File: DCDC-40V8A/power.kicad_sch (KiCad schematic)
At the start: 53 parts, among them Q1 CSD18533Q5A, Q2 CSD18533Q5A, Q3 CSD18533Q5A, Q4 CSD18533Q5A, U2 LGS5145EP, U3 MT3608, U4 GS2019-33TR5

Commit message: wip
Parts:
- added C25, C26: 100n, symbol Device:C
- added C27: 1u, symbol Device:C
- added C28, C29: 100n, Capacitor_SMD:C_0603_1608Metric, symbol Device:C
- added C30: 470n, Capacitor_SMD:C_0603_1608Metric, symbol Device:C
- added C31, C32: 100u, symbol Device:C_Polarized
- added R15, R16: 10, Resistor_SMD:R_0603_1608Metric, symbol Device:R
- C1, C8: value 22u -> 10u
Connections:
- net GND: now also C25.2, C26.2, C27.2, C28.2, C29.1, C31.2, C32.2
- net VBAT: now also C5.1
- net VCC: now also C25.1, C26.1, C27.1, C31.1, C32.1, R15.1; no longer C1.1, C2.1, C3.1, U1.30 (ACP)
- net at Q1.5 (D), R5.2: now also C1.1, C2.1, C3.1, R16.1; no longer U1.29 (ACN)
- net at C6.1, C7.1, C8.1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: no longer C5.1
- new net: C29.2, C30.2, R16.2, U1.29 (ACN)
- new net: C28.1, C30.1, R15.2, U1.30 (ACP)
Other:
- moved on the sheet: C1, C10, C11, C12, C13, C14, C15, C16, C17, C2, C3, C4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

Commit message: wip
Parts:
- added C44: 10u, symbol Device:C
- added C45: 100n, symbol Device:C
- added C46: 10u, Capacitor_SMD:C_0603_1608Metric, symbol Device:C
- added D5: SS26, Diode_SMD:D_SMA, symbol Diode:SS26
- added L4: 10u, symbol Device:L
- added R18: 51k, Resistor_SMD:R_0603_1608Metric, symbol Device:R
- added R19: 10k, Resistor_SMD:R_0603_1608Metric, symbol Device:R
- added U14: LGS5145EP, Package_SO:HSOP-8-1EP_3.9x4.9mm_P1.27mm_EP2.41x3.1mm_ThermalVias, symbol Regulator_Switching:LM5164DDA
- C20: value C -> 10u
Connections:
- net +5V: now also C46.1, L4.2, R18.1
- net GND: now also C44.2, C46.2, D5.2 (A), R19.2, U14.7 (GND), U14.9 (EP)
- net VCC: now also C44.1, U14.2 (VIN)
- net EN renamed MAIN_5V_EN
- new net: C45.1, U14.1 (BST)
- new net: C45.2, D5.1 (K), L4.1, U14.8 (SW)
- new net: R18.2, R19.1, U14.5 (FB)
- new net BAT_5V_EN: U14.3 (EN)
- no-connect marks 9 -> 11
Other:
- added sheet Charge Pump (charge_pump.kicad_sch)
- note added: "Vout -> 5V Buck (1A)"
- moved on the sheet: C18

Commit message: move adc MUX and discharge to new sheet
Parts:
- U1: value ~ -> (none)

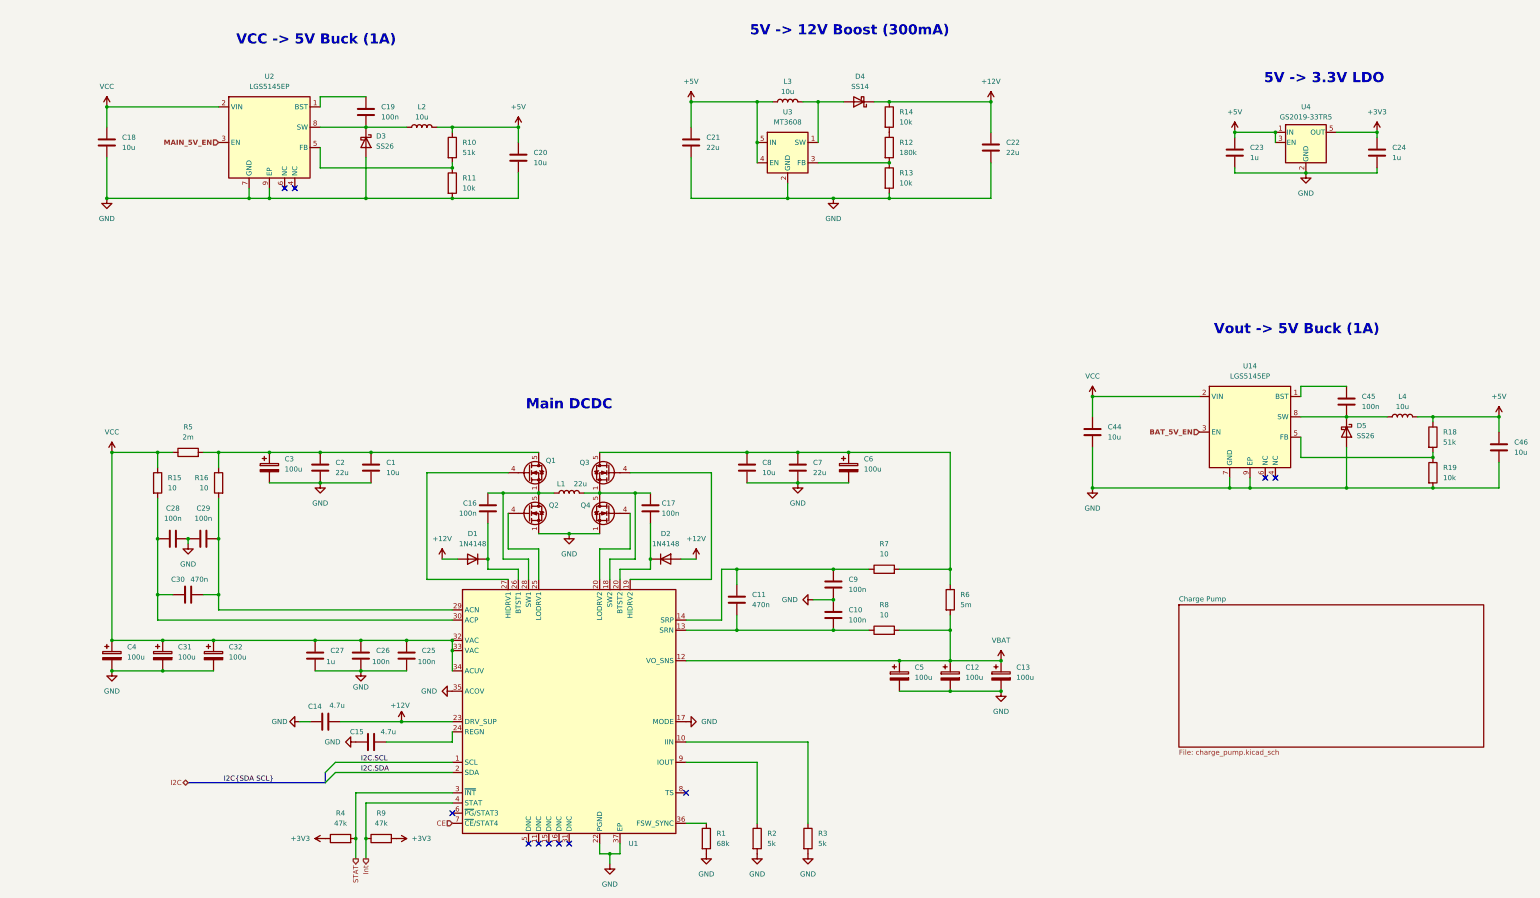
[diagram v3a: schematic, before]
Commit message: added discharge circuitry and help texts
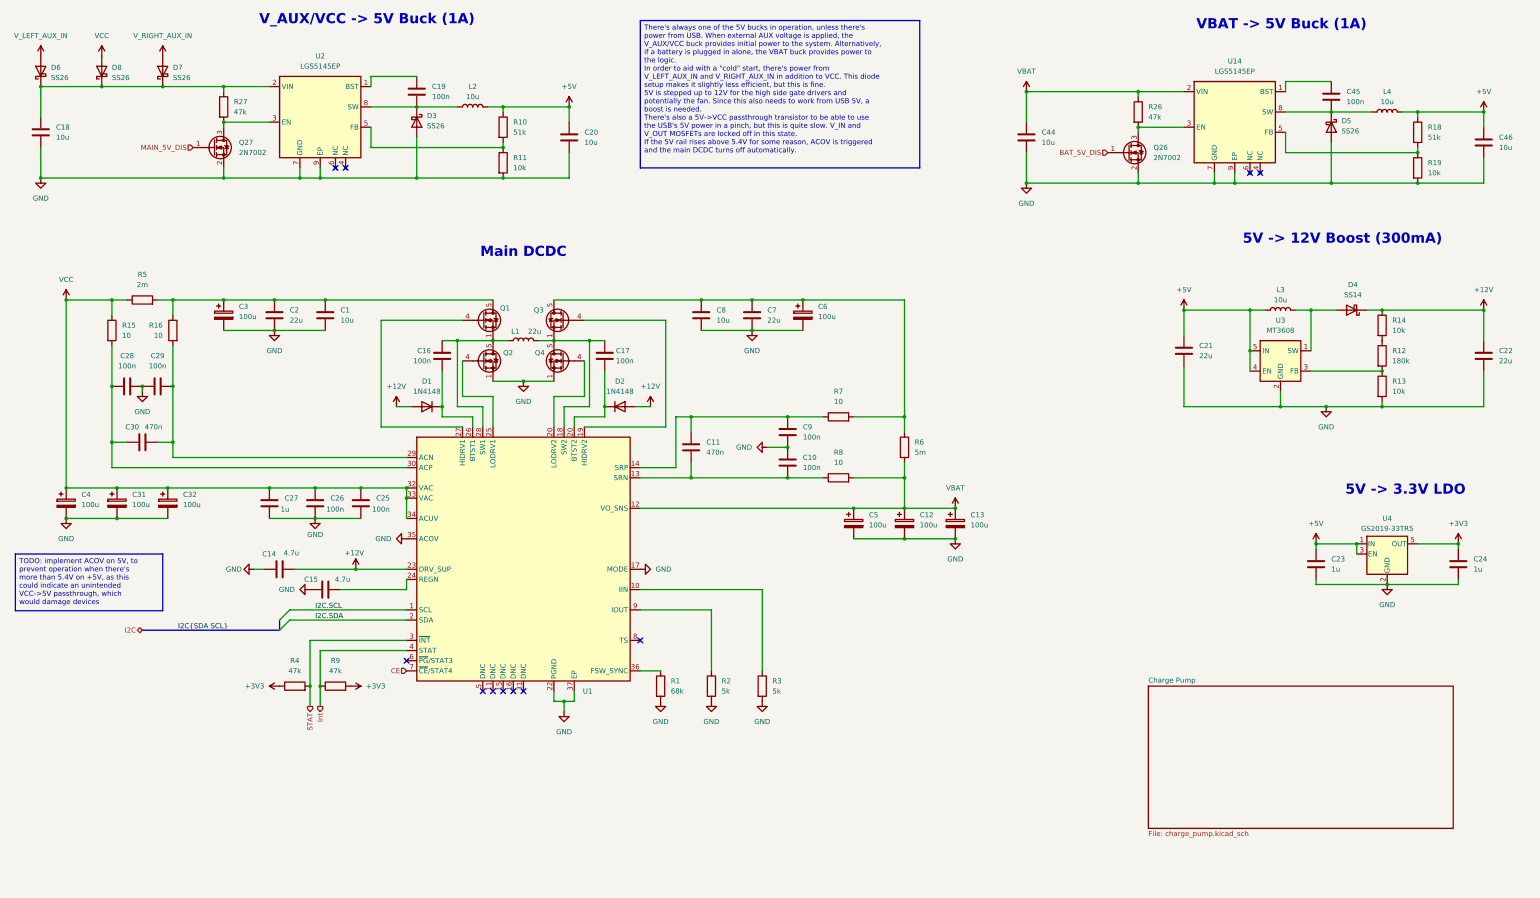
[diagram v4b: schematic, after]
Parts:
- added D6, D7, D8: SS26, Diode_SMD:D_SMA, symbol Diode:SS26
- added Q26, Q27: 2N7002, Package_TO_SOT_SMD:SOT-23, symbol Transistor_FET:2N7002
- added R26, R27: 47k, Resistor_SMD:R_0603_1608Metric, symbol Device:R
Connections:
- net GND: now also Q26.2 (S), Q27.2 (S)
- net VBAT: now also C44.1, U14.2 (VIN), R26.1
- net VCC: now also D8.2 (A); no longer C18.1, C44.1, U14.2 (VIN), U2.2 (VIN)
- net BAT_5V_EN: no longer names the net of U14.3 (EN)
- net BAT_5V_EN: now also Q26.3 (D), R26.2
- net MAIN_5V_EN: no longer names the net of U2.3 (EN)
- net MAIN_5V_EN: now also Q27.3 (D), R27.2
- new net: C18.1, D6.1 (K), D7.1 (K), D8.1 (K), R27.1, U2.2 (VIN)
- new net BAT_5V_DIS: Q26.1 (G)
- new net MAIN_5V_DIS: Q27.1 (G)
- new net V_LEFT_AUX_IN: D6.2 (A)
- new net V_RIGHT_AUX_IN: D7.2 (A)
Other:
- note added: "VBAT -> 5V Buck (1A)"
- note added: "V_AUX/VCC -> 5V Buck (1A)"
- note removed: "VCC -> 5V Buck (1A)"
- note removed: "Vout -> 5V Buck (1A)"
- moved on the sheet: C1, C10, C11, C12, C13, C14, C15, C16, C17, C18, C19, C2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

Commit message: wip
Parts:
- removed C46: 10u, Capacitor_SMD:C_0603_1608Metric, symbol Device:C
- removed D5: SS26, Diode_SMD:D_SMA, symbol Diode:SS26
- removed L4: 10u, symbol Device:L
- removed Q26: 2N7002, Package_TO_SOT_SMD:SOT-23, symbol Transistor_FET:2N7002
- removed R26: 47k, Resistor_SMD:R_0603_1608Metric, symbol Device:R
- removed U14: LGS5145EP, Package_SO:HSOP-8-1EP_3.9x4.9mm_P1.27mm_EP2.41x3.1mm_ThermalVias, symbol Regulator_Switching:LM5164DDA
- added D25, D26, D31: SS26, Diode_SMD:D_SMA, symbol Diode:SS26
- added D27, D28: 1N4148WS, Diode_SMD:D_SOD-323, symbol Diode:1N4148WS
- added Q21, Q56, Q57: BSS83P, Package_TO_SOT_SMD:SOT-23, symbol Transistor_FET:BSS83P
- added Q45, Q46, Q58, Q59: 2N7002, Package_TO_SOT_SMD:SOT-23, symbol Transistor_FET:2N7002
- added R166, R167, R168, R169, R170: 100k, Resistor_SMD:R_0603_1608Metric, symbol Device:R
- added R171: 2.2k, Resistor_SMD:R_0402_1005Metric, symbol Device:R
- added R84: R, Resistor_SMD:R_0402_1005Metric, symbol Device:R
- C44: value 10u -> 100n; footprint (none) -> Capacitor_SMD:C_0603_1608Metric
- C45: value 100n -> 10u; footprint (none) -> Capacitor_SMD:C_0402_1005Metric
- R18: value 51k -> 10k; footprint Resistor_SMD:R_0603_1608Metric -> Resistor_SMD:R_0402_1005Metric
- R19: value 10k -> 33k; footprint Resistor_SMD:R_0603_1608Metric -> Resistor_SMD:R_0402_1005Metric
- R27: value 47k -> 100k
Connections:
- net +5V: now also Q56.3 (D), R171.1; no longer R18.1
- net GND: now also R18.2, Q45.2 (S), Q46.2 (S), Q58.2 (S), Q59.2 (S), R166.2, R170.2, R84.2; no longer C44.2, R19.2, U1.35 (ACOV)
- net VBAT: no longer C44.1
- net VCC: now also C45.2, D27.2 (A), Q57.3 (D)
- net at C18.1, D6.1 (K), D7.1 (K)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: now also D31.1 (K), Q21.3 (D)
- net V_HI_DRV: now reaches C45.1
- net V_HI_DRV: now also D28.1 (K)
- net at R19.1: now also R171.2; no longer R18.2
- net MAIN_5V_DIS renamed 5V_DCDC_DIS
- net 5V_DCDC_DIS: now also R166.1
- new net: Q21.1 (G), R167.2, R168.1
- new net: Q57.1 (G), Q58.3 (D)
- new net: Q45.1 (G), Q46.3 (D), R169.2, R170.1
- new net: Q45.3 (D), R168.2
- new net: C44.1, D27.1 (K), D28.2 (A)
- new net: Q56.1 (G), Q59.3 (D)
- new net: Q56.2 (S), Q57.2 (S)
- new net +BAT_A: D25.2 (A)
- new net +BAT_B: D26.2 (A)
- new net ACOV: R18.1, R19.2, U1.35 (ACOV)
- new net BAL_PWR: D25.1 (K), D26.1 (K), Q21.2 (S), R167.1, R169.1
- new net BAT_DCDC_DIS: Q46.1 (G)
- new net Charge Pump/C-: C44.2
- new net PWR_5V_EN: Q58.1 (G), Q59.1 (G), R84.1
- new net V_XT60IN: D31.2 (A)
- no-connect marks 11 -> 9
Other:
- sheet Charge Pump ports: added C-, LV_IN, PWM_IN; removed none
- note added: "5V -> VCC passthrough"
- note added: "V_AUX/VCC/VBAT/V_BAL -> 5V Buck (1A)"
- note removed: "VBAT -> 5V Buck (1A)"
- note removed: "V_AUX/VCC -> 5V Buck (1A)"
- moved on the sheet: C19, C20, D3, L2, Q27, R10, R11, R27, U2

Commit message: wip before CP deletion
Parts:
- added R172: 100k, Resistor_SMD:R_0603_1608Metric, symbol Device:R
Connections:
- net BAT_DCDC_DIS: now also R172.1
- net GND: now also R172.2
- net V_XT60IN renamed V_EXT
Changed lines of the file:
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@@
 		)
 	)
-	(text_box "All the possible power sources are shorted together via diodes to create the VIN for the 5V DCDC. The battery source can be selectively turned off to prevent power the battery if there is VCC but VCC is lower than VBAT.\nIn order to aid with a \"cold\" start, there's power from V_LEFT_AUX_IN and V_RIGHT_AUX_IN in addition to VCC. This diode setup makes it slightly less efficient, but this is fine.\n5V is stepped up to 12V for the high side gate drivers and potentially the fan. Since this also needs to work from USB 5V, a boost is needed.\nThere's also a 5V->VCC passthrough transistor to be able to use the USB's 5V power in a pinch, but this is quite slow. V_LEFT and V_RIGHT MOSFETs are locked off in this state.\nIf the 5V rail rises above 5.4V for some reason, ACOV is triggered and the main DCDC turns off automatically."
+	(text_box "All the possible power sources are shorted together via diodes to create the VIN for the 5V DCDC. The battery source can be selectively turned off to prevent power the battery if there is VCC but VCC is lower than VBAT.\nIn order to aid with a \"cold\" start, there's power from V_LEFT_AUX_IN and V_RIGHT_AUX_IN in addition to VCC. This diode setup makes it slightly less efficient, but this is fine.\n5V is stepped up to 12V for the high side gate drivers and potentially the fan. Since this also needs to work from USB 5V, a boost is needed.\nThere's also a 5V->VCC passthrough transistor to be able to use the USB's 5V power in a pinch, but this is quite slow. V_EXT MOSFETs are locked off in this state.\nIf the 5V rail rises above 5.4V for some reason, ACOV is triggered and the main DCDC turns off automatically."
 		(exclude_from_sim no)
-		(at 323.85 27.94 0)
-		(size 69.85 36.83)
+		(at 323.85 30.48 0)
+		(size 69.85 32.5731)
 		(margins 0.9525 0.9525 0.9525 0.9525)
 		(stroke
@@
 	)
 	(junction
+		(at 71.12 58.42)
+		(diameter 0)
+		(color 0 0 0 0)
+	)
+	(junction
 		(at 246.38 68.58)
 		(diameter 0)
@@
 	)
 	(junction
+		(at 71.12 68.58)
+		(diameter 0)
+		(color 0 0 0 0)
+	)
+	(junction
 		(at 358.14 101.6)
 		(diameter 0)
@@
 	(wire
 		(pts
+			(xy 64.77 58.42) (xy 71.12 58.42)
+		)
+		(stroke
+			(width 0)
+			(type default)
+		)
+	)
+	(wire
+		(pts
 			(xy 90.17 195.58) (xy 90.17 200.66)
 		)
@@
 	(wire
 		(pts
+			(xy 71.12 68.58) (xy 88.9 68.58)
+		)
+		(stroke
+			(width 0)
+			(type default)
+		)
+	)
+	(wire
+		(pts
 			(xy 40.64 120.65) (xy 40.64 134.62)
 		)
@@
 	(wire
 		(pts
+			(xy 71.12 58.42) (xy 71.12 59.69)
+		)
+		(stroke
+			(width 0)
+			(type default)
+		)
+	)
+	(wire
+		(pts
+			(xy 71.12 58.42) (xy 81.28 58.42)
+		)
+		(stroke
+			(width 0)
+			(type default)
+		)
+	)
+	(wire
+		(pts
 			(xy 22.86 60.96) (xy 22.86 68.58)
 		)
@@
 	(wire
 		(pts
-			(xy 22.86 68.58) (xy 88.9 68.58)
+			(xy 22.86 68.58) (xy 71.12 68.58)
 		)
 		(stroke
@@
 	(wire
 		(pts
+			(xy 71.12 67.31) (xy 71.12 68.58)
+		)
+		(stroke
+			(width 0)
+			(type default)
+		)
+	)
+	(wire
+		(pts
 			(xy 135.89 99.06) (xy 93.98 99.06)
 		)
@@
 	(wire
 		(pts
+			(xy 81.28 58.42) (xy 81.28 63.5)
+		)
+		(stroke
+			(width 0)
+			(type default)
+		)
+	)
+	(wire
+		(pts
 			(xy 85.09 179.07) (xy 114.3 179.07)
 		)
@@
 	(hierarchical_label "BAT_DCDC_DIS"
 		(shape input)
-		(at 81.28 63.5 180)
+		(at 64.77 58.42 180)
 		(effects
 			(font
@@
 			)
 		)
-		(property "Value" "V_XT60IN"
+		(property "Value" "V_EXT"
 			(at 68.58 33.02 0)
 			(show_name no)
@@
 					(unit 1)
 				)
+			)
+		)
+	)
+	(symbol
+		(lib_id "Device:R")
+		(at 71.12 63.5 0)
+		(unit 1)
+		(body_style 1)
+		(exclude_from_sim no)
+		(in_bom yes)
+		(on_board yes)
+		(in_pos_files yes)
+		(dnp no)
+		(fields_autoplaced yes)
+		(property "Reference" "R172"
+			(at 73.66 62.2299 0)
+			(show_name no)
+			(do_not_autoplace no)
+			(effects
+				(font
+					(size 1.27 1.27)
+				)
+				(justify left)
+			)
+		)
+		(property "Value" "100k"
+			(at 73.66 64.7699 0)
+			(show_name no)
+			(do_not_autoplace no)
+			(effects
+				(font
+					(size 1.27 1.27)
+				)
+				(justify left)
+			)
+		)
+		(property "Footprint" "Resistor_SMD:R_0603_1608Metric"
+			(at 69.342 63.5 90)
+			(hide yes)
+			(show_name no)
+			(do_not_autoplace no)
+			(effects
+				(font
+					(size 1.27 1.27)
+				)
+			)
+		)
+		(property "Datasheet" ""
+			(at 71.12 63.5 0)
+			(hide yes)
+			(show_name no)
+			(do_not_autoplace no)
+			(effects
+				(font
+					(size 1.27 1.27)
+				)
+			)
+		)
+		(property "Description" "Resistor"
+			(at 71.12 63.5 0)
+			(hide yes)
+			(show_name no)
+			(do_not_autoplace no)
+			(effects
+				(font
+					(size 1.27 1.27)
+				)
+			)
+		)
+		(pin "1"
+		)
+		(pin "2"
+		)
+		(instances
+			(project "DCDC-40V8A"
+				(path "/c2f330be-6ca8-4ed0-86db-c2e1bfb68425/e02b7f28-305a-4574-afeb-14db4b4e1edd"
+					(reference "R172")
+					(unit 1)
+				)

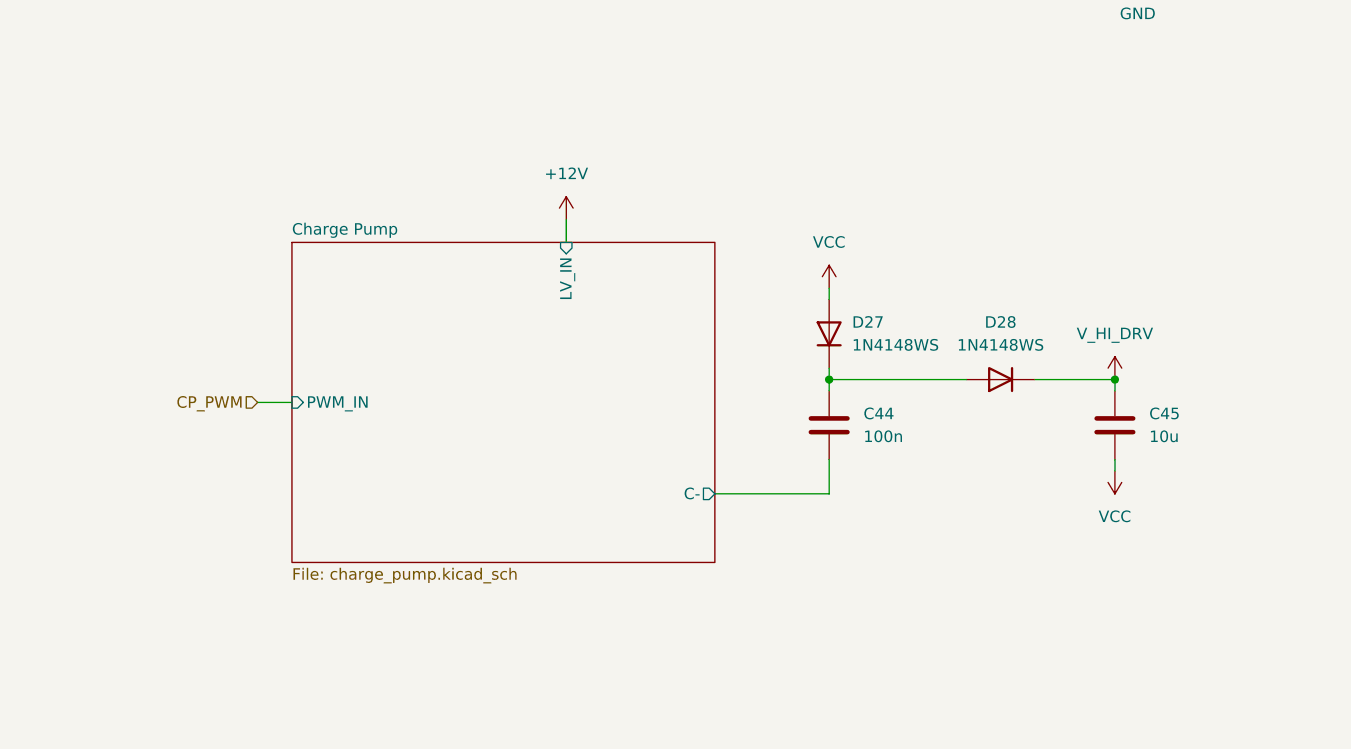
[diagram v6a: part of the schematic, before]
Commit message: delete unnecessary CP
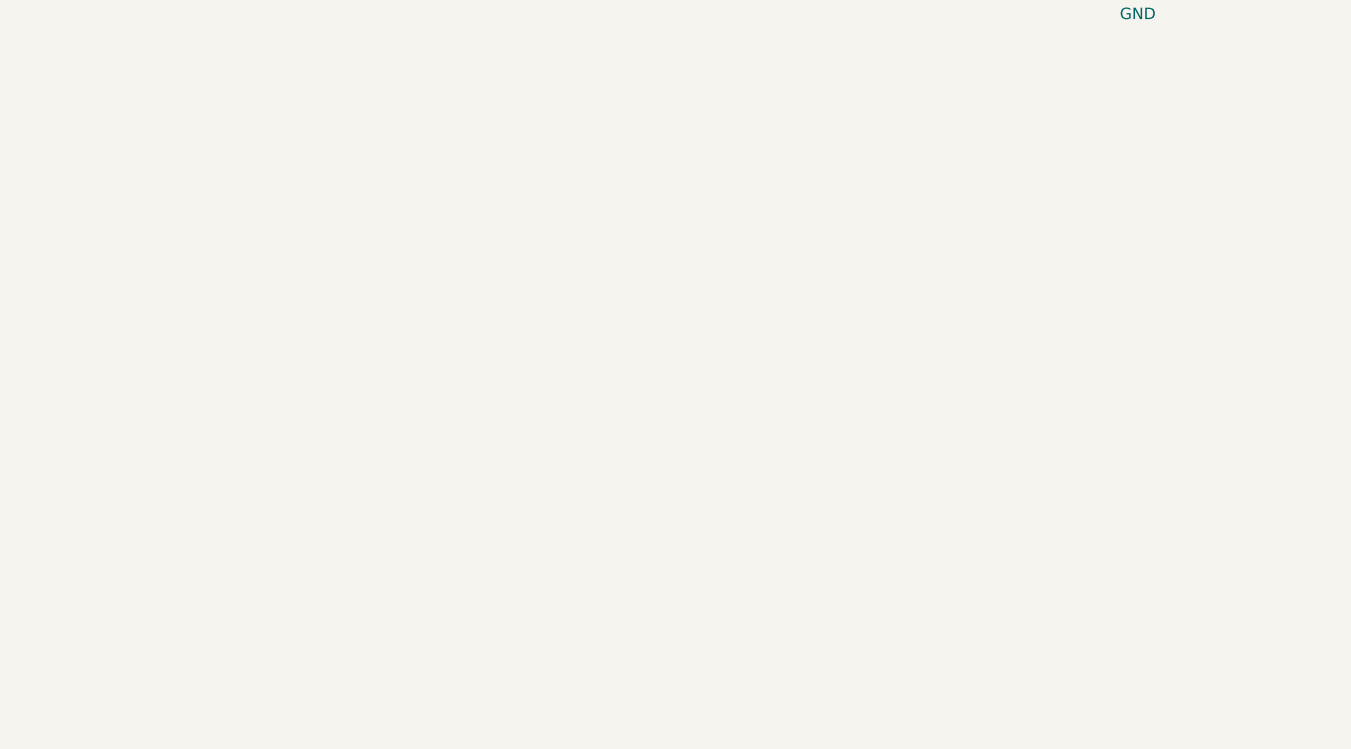
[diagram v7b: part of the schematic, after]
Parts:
- removed C44: 100n, Capacitor_SMD:C_0603_1608Metric, symbol Device:C
- removed C45: 10u, Capacitor_SMD:C_0402_1005Metric, symbol Device:C
- removed D27, D28: 1N4148WS, Diode_SMD:D_SOD-323, symbol Diode:1N4148WS
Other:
- removed sheet Charge Pump

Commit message: renumbering
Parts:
- R27: renamed from R84; value R -> 10k
- renumbered C19 to C1, C21 to C10, C16 to C11, C17 to C12, C22 to C13, C28 to C14, C29 to C15, C9 to C16, C30 to C17, C11 to C18, C10 to C19, C18 to C2, C4 to C20, C31 to C21, C32 to C22, C27 to C23, C26 to C24, C5 to C26, C12 to C27, C13 to C28, C23 to C29, C20 to C3, C24 to C30, C14 to C31, C15 to C32, C3 to C4, C2 to C5, C1 to C6, C8 to C7, C7 to C8, C6 to C9, D25 to D1, D2 to D10, D26 to D2, D6 to D3, D8 to D4, D7 to D5, D31 to D6, D3 to D7, D4 to D8, D1 to D9, L2 to L1, L3 to L2, L1 to L3, Q21 to Q1, Q56 to Q10, Q58 to Q11, Q59 to Q12, Q27 to Q2, Q46 to Q3, Q45 to Q4, Q1 to Q5, Q3 to Q6, Q2 to Q7, Q4 to Q8, Q57 to Q9, R169 to R1, R5 to R10, R14 to R11, R15 to R12, R16 to R13, R12 to R14, R13 to R15, R7 to R16, R6 to R17, R8 to R18, R171 to R19, R167 to R2, R19 to R20, R18 to R21, R4 to R22, R9 to R23, R1 to R24, R2 to R25, R3 to R26, R27 to R3, R168 to R4, R10 to R5, R172 to R6, R170 to R7, R166 to R8, R11 to R9, U2 to U1, U3 to U2, U4 to U3, U1 to U4
